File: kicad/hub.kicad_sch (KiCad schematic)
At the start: 43 parts, among them U201 USB5807, Y201 25Mhz

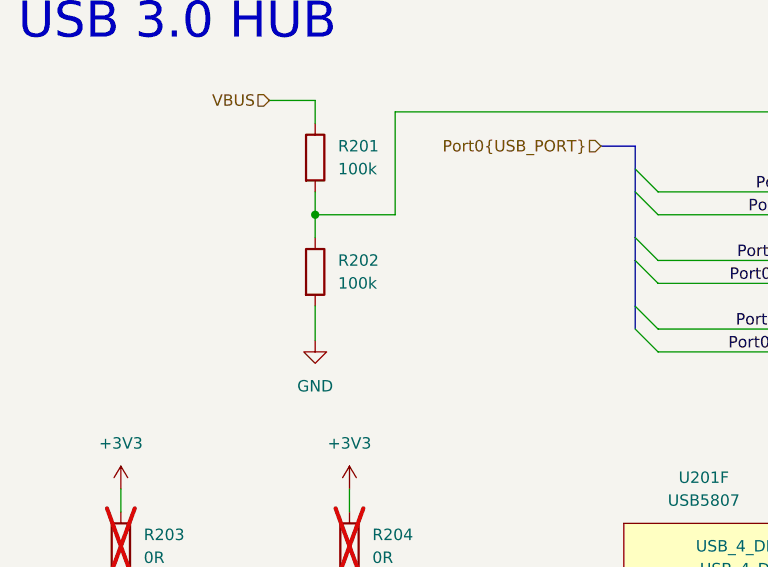
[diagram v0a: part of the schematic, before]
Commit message: Update Pulldown resitor value
It should not be 1:1, but 1:2 ratio per reference design
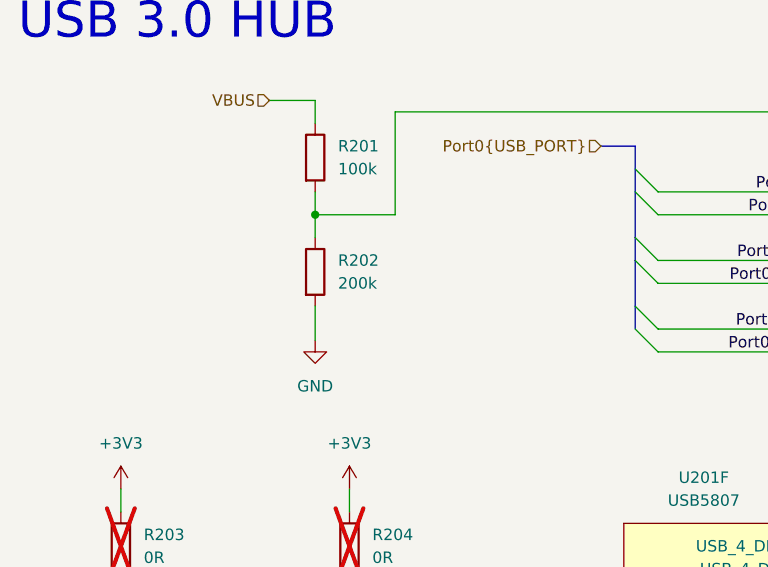
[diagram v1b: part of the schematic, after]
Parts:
- R202: value 100k -> 200k
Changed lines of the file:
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@@
 			)
 		)
-		(property "Value" "100k"
+		(property "Value" "200k"
 			(at 49.53 45.7199 0)
 			(effects
